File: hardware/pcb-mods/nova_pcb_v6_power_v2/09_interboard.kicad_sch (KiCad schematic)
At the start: 1 part, among them J20 IB_2x06

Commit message: pcb(v6-power-v2): backfill MPN + Manufacturer fields — 100% BOM coverage
All 50 BOM components now carry MPNs from the verified order list:
Yageo RC0603 resistor set (R14 470k = Vishay CRCW0603 DigiKey sub),
Nichicon UPW1E bulk caps, Bourns SRR1260-220M, Infineon IRLB3034PBF,
onsemi BSS138 x3, TI LM393DR, Pololu buck modules (off-board),
GODIY INA226 20A R002 modules with I2C addresses in Manufacturer field,
AMASS XT60H/XT30U, JST B3B-XH-A, Adam Tech BHR-12-VUA, Sullins headers.
ERC: 0 errors (1 expected V7V5_ARM warning). kicad-happy bom_lock: pass.

Co-Authored-By: Claude Fable 5 <noreply@anthropic.com>
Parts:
- J20: MPN (none) -> BHR-12-VUA; Manufacturer (none) -> Adam Tech (DigiKey 10414809)
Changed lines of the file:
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@@
+			)
+		)
+		(property "Manufacturer" "Adam Tech (DigiKey 10414809)" (at 0 0 0)
+			(effects
+				(font
+					(size 1.27 1.27)
+				)
+				(hide yes)
+			)
+		)
+		(property "MPN" "BHR-12-VUA" (at 0 0 0)
+			(effects
+				(font
+					(size 1.27 1.27)
+				)
+				(hide yes)
 			)
 		)

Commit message: pcb(v6-power-v2): correct C1-C5 to FymuSing (as purchased) + DigiKey PNs from order CSV
Verified against Complete_Digikey_Order_NOVA.csv (16 lines, all match):
R14 470k confirmed Vishay CRCW0603470KFKEA (541-470KHCT-ND).
C1-C5 corrected Nichicon->FymuSing 1000uF/25V (Amazon purchase, 10x17mm).
Remaining 23 parts without DigiKey PN are Amazon/Pololu/AMASS sourced.

Co-Authored-By: Claude Fable 5 <noreply@anthropic.com>
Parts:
- J20: DigiKey (none) -> 2057-BHR-12-VUA-ND
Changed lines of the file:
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@@
+			)
+		)
+		(property "DigiKey" "2057-BHR-12-VUA-ND" (at 0 0 0)
+			(effects
+				(font
+					(size 1.27 1.27)
+				)
+				(hide yes)
 			)
 		)

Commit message: pcb(v6-power-v2): AssemblyOrder fields + assembly-sequenced iBOM
15-step hand-solder sequence (flat->tall, SMD bottom cluster -> THT top):
0603s -> SOT-23 -> SOIC -> L1 -> INA headers -> headers/JST/IDC ->
screw blocks -> XT30 -> XT60 -> Q1 (Step 10a test first) -> 470uF -> 1000uF.
bom/ibom_assembly.html groups by AssemblyOrder via netlist extra-data.

Co-Authored-By: Claude Fable 5 <noreply@anthropic.com>
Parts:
- J20: AssemblyOrder (none) -> 09 THT IDC shrouded
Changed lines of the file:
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@@
+			)
+		)
+		(property "AssemblyOrder" "09 THT IDC shrouded" (at 0 0 0)
+			(effects
+				(font
+					(size 1.27 1.27)
+				)
+				(hide yes)
 			)
 		)

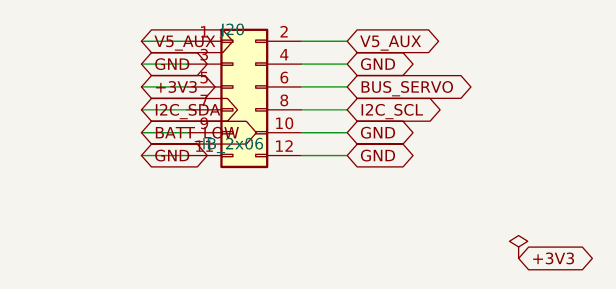
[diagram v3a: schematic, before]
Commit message: Chassis + leg_v6 CAD: no-drill assembly, leg fault audit (LA-1..28 + #47), fastener + gate hardening (#48)
* power board: arm Phase-4 routed + cleaned + fresh gerbers (fab-ready)

Completes the power board (blocker B1):
- U5.EN routed on EN_BUCKS (re-gate now realized on the board).
- V7V5_ARM 3mm, BATT_NEG/VBAT long runs 3mm, 21 high-current pads solid
  zone-connection (current-capacity fixes; TO-220/SW1 escapes left at 1.3mm).
- Removed the duplicate U12 + J14 (F8 UUID-mismatch artifacts) and the full
  orphan dangling-track chain they left behind.
- DRC: 0 hard, 0 unconnected, 0 dangling (10 cosmetic silk/lib only).
- Gerbers regenerated; fab_gate GO on both boards (J20 cross-board match OK).

DNP roster correct (U5 arm buck, U12 arm INA = Phase-4 reserve).

Co-Authored-By: Claude Opus 4.8 <noreply@anthropic.com>

* audit fixes 2026-06-18: NaN guard, pinout/battery/LVC doc sync, STATUS audit block

- main.cpp: NaN guard on commanded position (was UB (uint16_t)NaN -> 0 slam)
- teensy firmware/README.md: pinout table corrected to match main.cpp/PCB v6 (Serial1 0/1, E-stop 5, batt 4, active-LOW OE)
- power-budget.md + BOM.md: battery 4000->6000mAh (real Ovonic packs) + runtime/charge recompute
- BOM.md: bus driver order line -> SN74LVC125A (must be LVC, not 74HC125)
- STATUS.md: cross-domain audit section (open misalignments, weak points, questions)

Co-Authored-By: Claude Opus 4.8 <noreply@anthropic.com>

* docs: add servo-bus half-duplex timing bench checklist (pre-power-on §10)

Co-Authored-By: Claude Opus 4.8 <noreply@anthropic.com>

* docs: battery 4000->6000mAh sweep across secondary docs + STATUS CI-note fix

- 6000mAh 4S Ovonic (real pack) in cad-tooling, notes-qol (SoC math 5400mAh),
  order-list (bag), wiring diagram, README charger note, patterns pocket label
- dimensions.md + patterns.md: physical box/pocket dims flagged RE-MEASURE
  (6000mAh pack is larger; old 4000mAh dims kept as reference, not as truth)
- STATUS.md: corrected CI note (ros-pytest.yml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
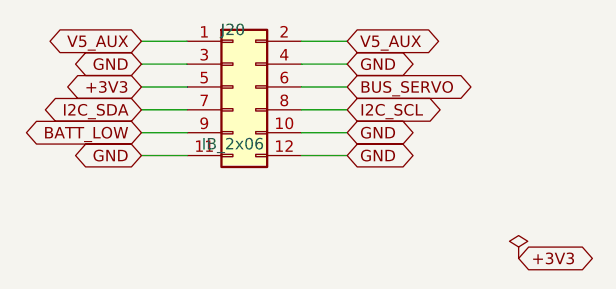
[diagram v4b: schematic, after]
